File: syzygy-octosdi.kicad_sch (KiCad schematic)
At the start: 13 parts, among them CN1 QTH-020-01-F-D-DP-A, X1 SX7DF148_500B20F30DNN

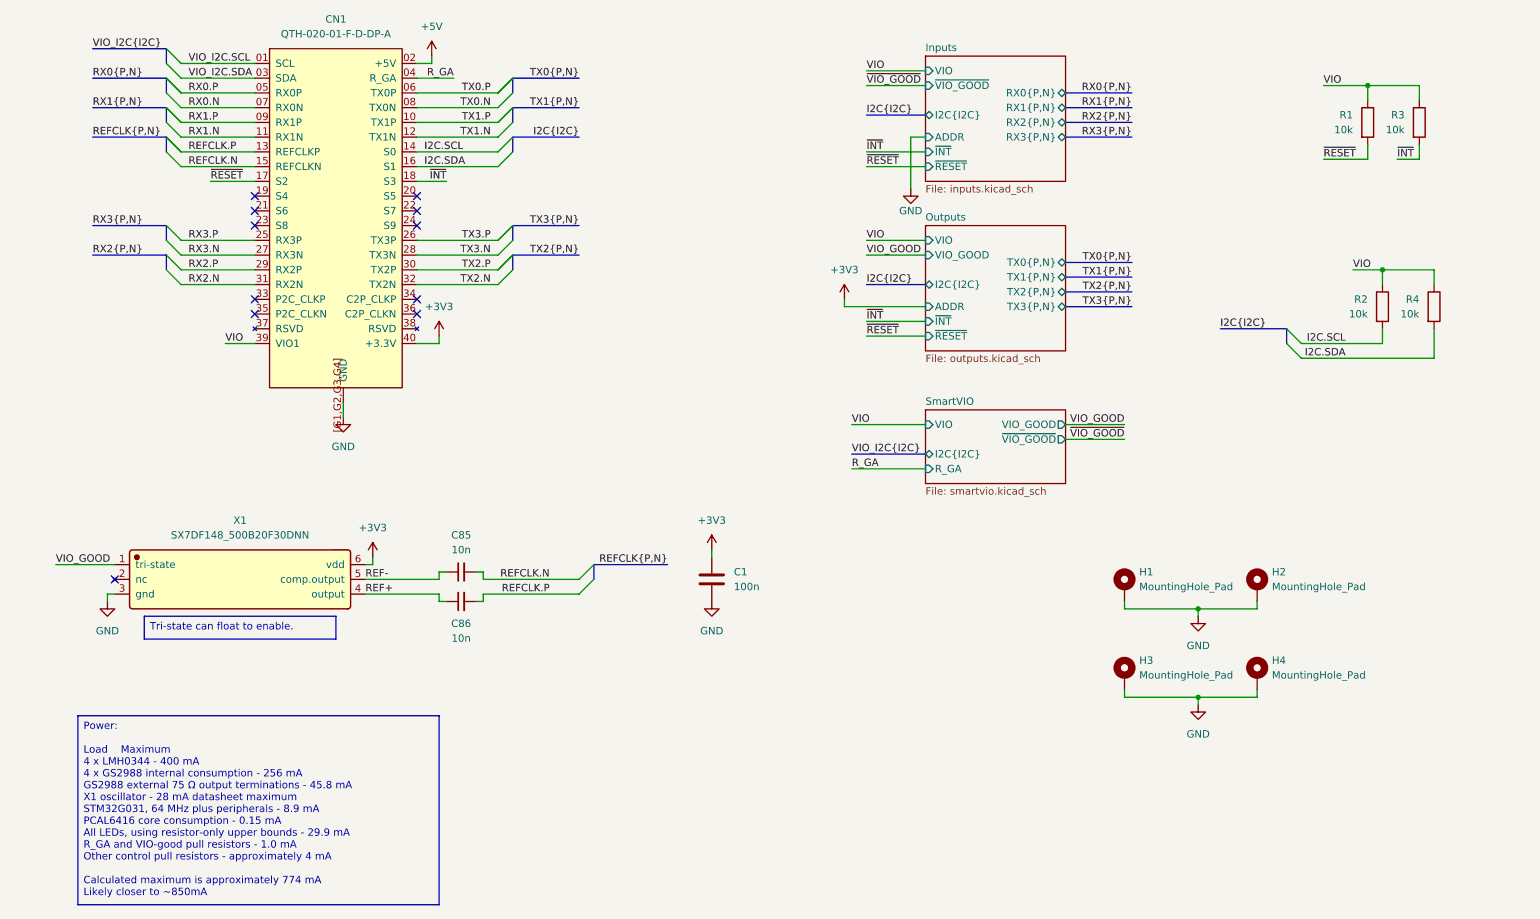
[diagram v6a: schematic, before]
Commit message: add power led and test points
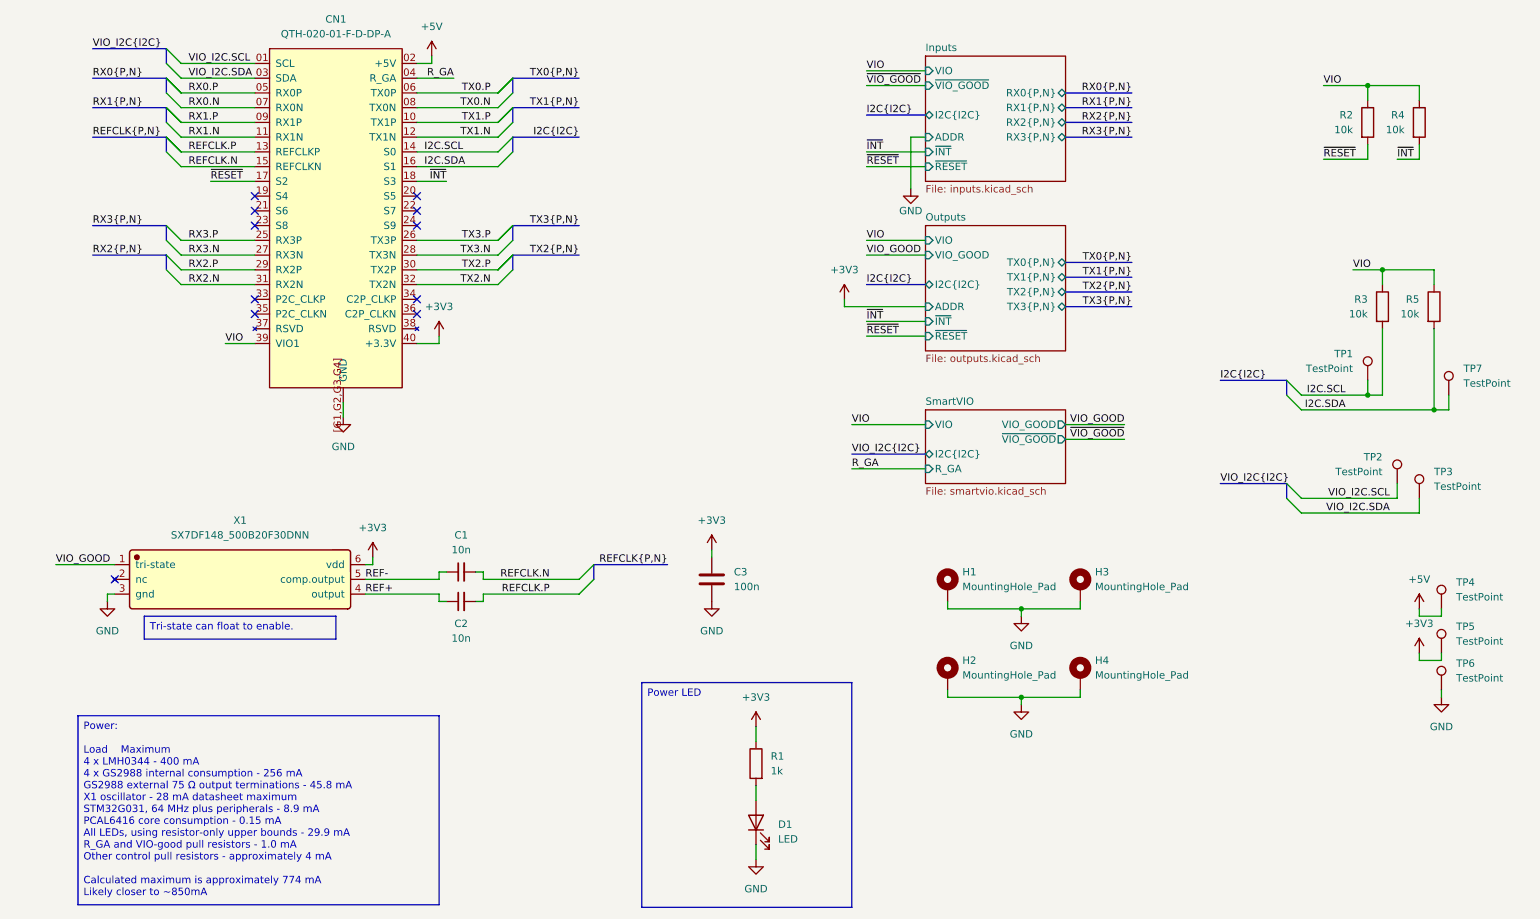
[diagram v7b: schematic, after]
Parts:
- added D1: LED, LED_SMD:LED_0603_1608Metric, symbol Device:LED
- added R1: 1k, Resistor_SMD:R_0603_1608Metric, symbol Device:R
- added TP1, TP2, TP3, TP4, TP5, TP6, TP7: TestPoint, TestPoint:TestPoint_Pad_D1.0mm, symbol Connector:TestPoint
- renumbered C85 to C1, C86 to C2, C1 to C3, H3 to H2, H2 to H3, R1 to R2, R2 to R3, R3 to R4, R4 to R5
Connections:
- net +3V3: now also R1.1, TP5.1
- net +5V: now also TP4.1
- net GND: now also D1.1 (K), TP6.1
- net I2C.SCL: now also TP1.1
- net I2C.SDA: now also TP7.1
- net VIO_I2C.SCL: now also TP2.1
- net VIO_I2C.SDA: now also TP3.1
- new net: D1.2 (A), R1.2
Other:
- moved on the sheet: H1, H2, H3, H4

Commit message: check against jlcpcb capabilities
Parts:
- C1, C2: KiLib_Generator (none) -> SMD_2terminal_chip_molded
- TP1, TP2, TP3, TP4, TP5, TP6, TP7: now left out of the parts list
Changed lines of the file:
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@@
 			)
 		)
+		(property "KiLib_Generator" "SMD_2terminal_chip_molded"
+			(at 95.25 135.89 0)
+			(hide yes)
+			(show_name no)
+			(do_not_autoplace no)
+			(effects
+				(font
+					(size 1.27 1.27)
+				)
+			)
+		)
 		(pin "2"
 		)
@@
 			)
 		)
+		(property "KiLib_Generator" "SMD_2terminal_chip_molded"
+			(at 95.25 130.81 0)
+			(hide yes)
+			(show_name no)
+			(do_not_autoplace no)
+			(effects
+				(font
+					(size 1.27 1.27)
+				)
+			)
+		)
 		(pin "2"
 		)
@@
 		(body_style 1)
 		(exclude_from_sim no)
-		(in_bom yes)
+		(in_bom no)
 		(on_board yes)
 		(in_pos_files yes)
@@
 		(body_style 1)
 		(exclude_from_sim no)
-		(in_bom yes)
+		(in_bom no)
 		(on_board yes)
 		(in_pos_files yes)
@@
 		(body_style 1)
 		(exclude_from_sim no)
-		(in_bom yes)
+		(in_bom no)
 		(on_board yes)
 		(in_pos_files yes)
@@
 		(body_style 1)
 		(exclude_from_sim no)
-		(in_bom yes)
+		(in_bom no)
 		(on_board yes)
 		(in_pos_files yes)
@@
 		(body_style 1)
 		(exclude_from_sim no)
-		(in_bom yes)
+		(in_bom no)
 		(on_board yes)
 		(in_pos_files yes)
@@
 		(body_style 1)
 		(exclude_from_sim no)
-		(in_bom yes)
+		(in_bom no)
 		(on_board yes)
 		(in_pos_files yes)
@@
 		(body_style 1)
 		(exclude_from_sim no)
-		(in_bom yes)
+		(in_bom no)
 		(on_board yes)
 		(in_pos_files yes)
